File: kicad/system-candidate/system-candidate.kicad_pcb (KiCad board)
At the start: 4 copper layers, 154 x 81 mm, 269 parts, among them J1 691137710002 2P 5.00mm, J2 Auxiliary 12V, J3 Differential audio, J301 T1_SECONDARY, J4 Control 2x4: 3V3 RESET FAULT 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, J401 START_BUTTON, J5 B2P-VH(LF)(SN), J6 GND braid solder bond - NO mo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, J7 B7B-XH-A(LF)(SN), J8 FAN 12V, K501 G6K-2F DC12, Q501 MMBT3904, Q502 MMBT3904, Q601 BCP56, Q602 BCP53, Q603 BSS138, Q701 BSS138, Q702 BSS138, Q703 BSS138, Q704 BSS138, Q705 BSS138, Q706 BSS138, Q707 AO3400A, U1 TPA3255DDV, U2 OPA1656ID, U3 OPA1656ID, U302 LM5164DDA, U303 TPS3700DDC, U401 LP2985-33, U402 TPS3808G33, U403 TPS3808G33, U404 TPS3808G33, U405 74LVC1G14, U406 74LVC2G74, U407 74LVC2G74, U408 74LVC1G32, U409 74LVC1G07, U410 74LVC1G08, U411 74LVC1G06, U412 TPS3700DDC, U413 TPS3700DDC, U414 TPS3808G33, U415 74LVC1G08, U416 TPS3808G33, U417 74LVC2G74, U418 74LVC1G32, U419 74LVC1G07, U501 TPS3700DDC, U502 TPS3700DDC, U503 TMUX6219, U504 TPS3700DDC

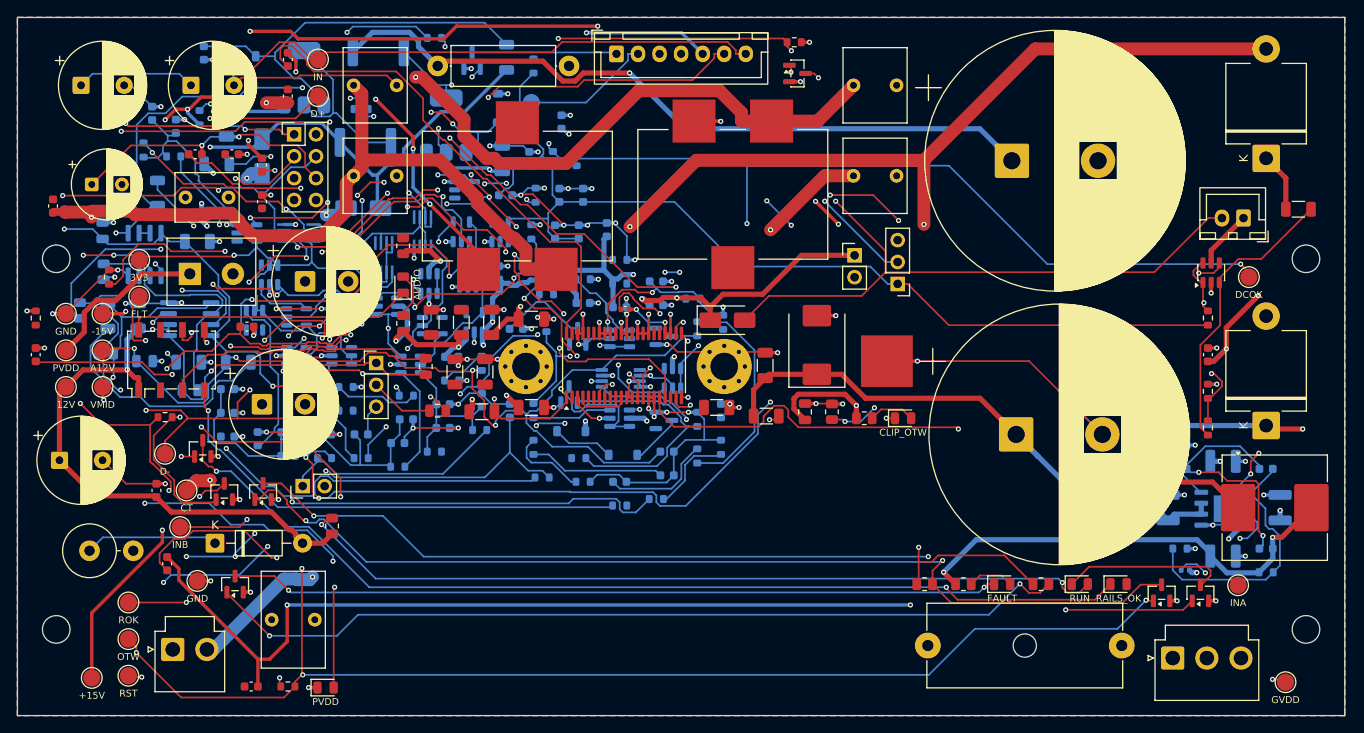
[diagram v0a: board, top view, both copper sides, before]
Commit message: feat(pcb): placement afrouxado em volta do U1 e nova rota (D-034)
- anel livre de 3 mm ao redor do TPA3255; lógica iso/seq/dbg afastada
- rota nova + passada --resume: 3.343 trilhas, 448 vias
- ERC 0, DRC 0 violações, paridade 0; conexões abertas 58 -> 6
- VMID colado à borda removido; PWM_AC 39-40 e PWM_BD 27-28 unidos no pad
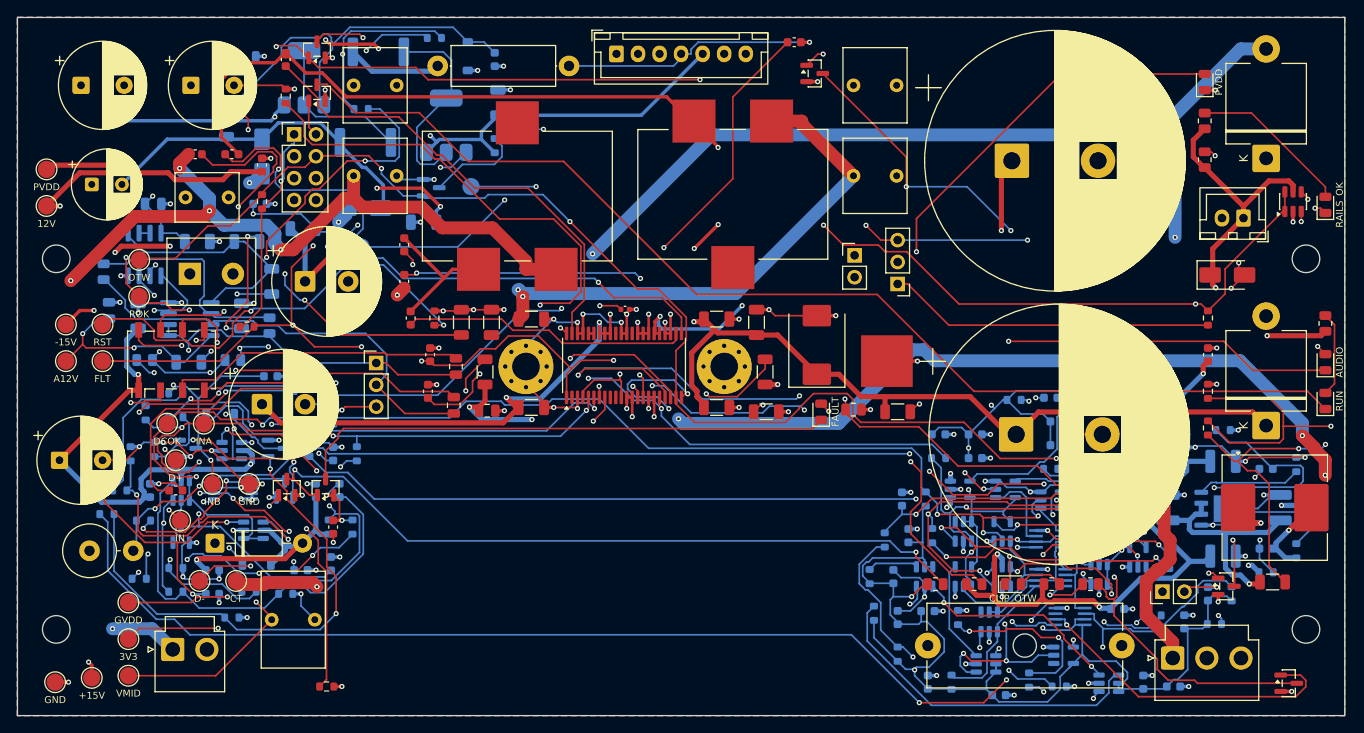
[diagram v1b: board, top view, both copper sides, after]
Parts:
- moved R404 136.3 mm to (160.9, 86.9)
- moved TP118 134.6 mm to (32.9, 87.9)
- moved TP123 126.6 mm to (37.4, 67.1)
- moved D701 123.9 mm to (157.8, 27.5), turned to 90 degrees
- moved TP127 121.5 mm to (41.6, 67.1)
- moved C409 118.3 mm to (150.6, 69.9), turned to 0 degrees
- moved Q702 117.8 mm to (54.8, 28.8)
- moved R703 117.6 mm to (171.8, 55.5)
- moved C406 114.3 mm to (154.1, 97.6)
- moved U409 110.0 mm to (150.0, 82.6), turned to 90 degrees
- moved R430 108.9 mm to (128.4, 97.1), turned to 90 degrees
- moved D704 107.4 mm to (171.8, 60.0)
- moved U403 101.6 mm to (146.6, 97.2)
- moved C402 100.6 mm to (144.9, 64.4)
- moved J401 100.5 mm to (152.8, 86.6)
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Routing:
- net /AUDIO_EN: track 0.00 -> 131.3 mm, vias 0 -> 8
- net /RAILS_OK: track 195.0 -> 325.3 mm, vias 12 -> 13
- net /CLIP_OTW: track 320.6 -> 196.3 mm, vias 8 -> 4
- net /GVDD_AB: track 225.4 -> 101.5 mm
- net /RELAY_DRV: track 39.1 -> 160.3 mm, vias 0 -> 4
- net /LED_RUN_K: track 19.3 -> 132.6 mm
- net /RESET: track 249.8 -> 145.9 mm, vias 10 -> 5
- net /START_DEB: track 121.9 -> 26.6 mm, vias 6 -> 2
- net /T1_CT: track 131.7 -> 223.1 mm, vias 1 -> 4
- net /INPUT_A_AC: track 11.3 -> 96.2 mm, vias 0 -> 5
- net /LED703_A: track 94.5 -> 9.85 mm, vias 2 -> 0
- net /DIVIDED: track 120.9 -> 37.4 mm
- net /VIO_3V3_EXTERNAL: track 108.5 -> 25.3 mm, vias 6 -> 1
- net /FREQ_ADJ: track 0.00 -> 71.5 mm, vias 0 -> 2
- net /SPK_N: track 206.5 -> 137.2 mm, vias 4 -> 3
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
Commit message: feat(pcb): saídas PWM do TPA3255 à mão, fechamento de conexões e make fab (D-035)
- escapes 0,25 mm, barramentos PWM_AC (F.Cu 1,0 mm) e PWM_BD (B.Cu 0,6 mm),
  1,5 mm até L1/L2; C8 movido para B.Cu sob o U1
- close_open_connections.py: A* em F/In2/B, aceita ligação só sem erro DRC novo
- export_fab.py / make fab: Gerber, drill, CPL, BOM, PDF, gabarito 1:1, SHA256
- ERC 0, DRC 0 erros, paridade 0; 9 conexões de sinal para o KiCad interativo
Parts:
- C8: moved to B.Cu
- moved C8 6.60 mm to (91.5, 60.4), turned to 90 degrees
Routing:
- net /LED_RUN_K: track 132.6 -> 0.09 mm
- net /FAULT: track 195.3 -> 96.0 mm, vias 9 -> 6
- net /BST_D: track 72.1 -> 1.17 mm, vias 2 -> 0
- net /BST_B: track 54.7 -> 0.02 mm
- net /SPK_N_SNUB: track 54.2 -> 0.00 mm, vias 3 -> 0
- net /CLIP_OTW: track 196.3 -> 150.2 mm, vias 4 -> 3
- net /VBG: track 39.9 -> 0.74 mm, vias 2 -> 0
- net /GND: track 1001.0 -> 975.1 mm, vias 134 -> 132
- net /PWM_AC: track 17.1 -> 40.9 mm, vias 0 -> 2
- net /C_START: track 19.4 -> 2.57 mm, vias 2 -> 1
- net /AUX_RAW: track 458.1 -> 473.4 mm, vias 16 -> 18
- net /PWM_BD: track 110.0 -> 96.5 mm, vias 5 -> 4
- net /SPK_P: track 141.2 -> 153.8 mm, vias 5 -> 7
- net /AUDIO_EN: track 131.3 -> 140.5 mm, vias 8 -> 13
- net /PVDD: track 395.5 -> 391.4 mm
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
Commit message: fix(pcb): close routing and verify nominal fit
Correct TPA placement and TP127/R506 connectivity.\nPreserve OEM fit assumptions and explicit fabrication gates.\nSync documentation, renders, tasks and GitHub mirrors.\n\nValidate ERC/DRC/parity and 138 local tests.\n\nRefs #3, #7, #8, #10, #11
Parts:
- C10, C13, C16, C17, C18, C19, C2, C4, C5, C6, C7, C9: moved to B.Cu
- moved C19 56.9 mm to (97.2, 58.2), turned to 90 degrees
- moved C7 55.2 mm to (92.4, 63.4)
- moved C17 47.2 mm to (85.6, 57.1)
- moved C6 45.1 mm to (88.9, 62.7), turned to 90 degrees
- moved C2 44.6 mm to (85.4, 62.0)
- moved C5 43.8 mm to (97.8, 64.2)
- moved C18 29.5 mm to (95.0, 57.1)
- moved C9 28.2 mm to (95.7, 61.1)
- moved C16 21.8 mm to (83.0, 58.4)
- moved C4 15.8 mm to (83.5, 61.5)
- moved C10 11.1 mm to (92.6, 58.1), turned to -90 degrees
- moved C13 11.1 mm to (88.1, 58.1), turned to -90 degrees
- moved C8 5.81 mm to (92.6, 66.1)
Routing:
- net /VMID: track 166.2 -> 355.5 mm, vias 10 -> 17
- net /LED_RUN_K: track 0.09 -> 135.8 mm, vias 0 -> 2
- net /FAULT: track 96.0 -> 183.1 mm, vias 6 -> 12
- net /AVDD: track 76.2 -> 1.07 mm, vias 3 -> 1
- net /SPK_N_SNUB: track 0.00 -> 62.5 mm, vias 0 -> 7
- net /PVDD: track 391.4 -> 453.5 mm, vias 12 -> 18
- net /DVDD_INTERNAL: track 60.6 -> 4.33 mm, vias 3 -> 2
- net /PWM_BD: track 96.5 -> 41.4 mm, vias 4 -> 6
- net /CLIP_OTW: track 150.2 -> 198.7 mm, vias 3 -> 4
- net /BST_C: track 33.0 -> 1.09 mm, vias 0 -> 1
- net /DC_OK: track 147.0 -> 177.5 mm, vias 5 -> 9
- net /GVDD_CD: track 72.0 -> 101.4 mm, vias 4 -> 6
- net /BST_A: track 21.7 -> 2.12 mm, vias 2 -> 1
- net /AUDIO_EN: track 140.5 -> 157.7 mm
- net /AUX_RAW: track 473.4 -> 456.9 mm, vias 18 -> 20
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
